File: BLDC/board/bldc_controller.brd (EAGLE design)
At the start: 104.1 x 76.8 mm, 113 parts, among them IC1 DRV8301, IC2 OPA2374, IC3 AS 5134, IC5 TPS51103, M1 FRDM-KL05Z, M2 MBED_NXP_LPC1768, Q1 MOSFET-NCHANNELSMD, Q2 MOSFET-NCHANNELSMD, Q3 P-CHANNEL-MOSFETTO252, Q4 SLPS388A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

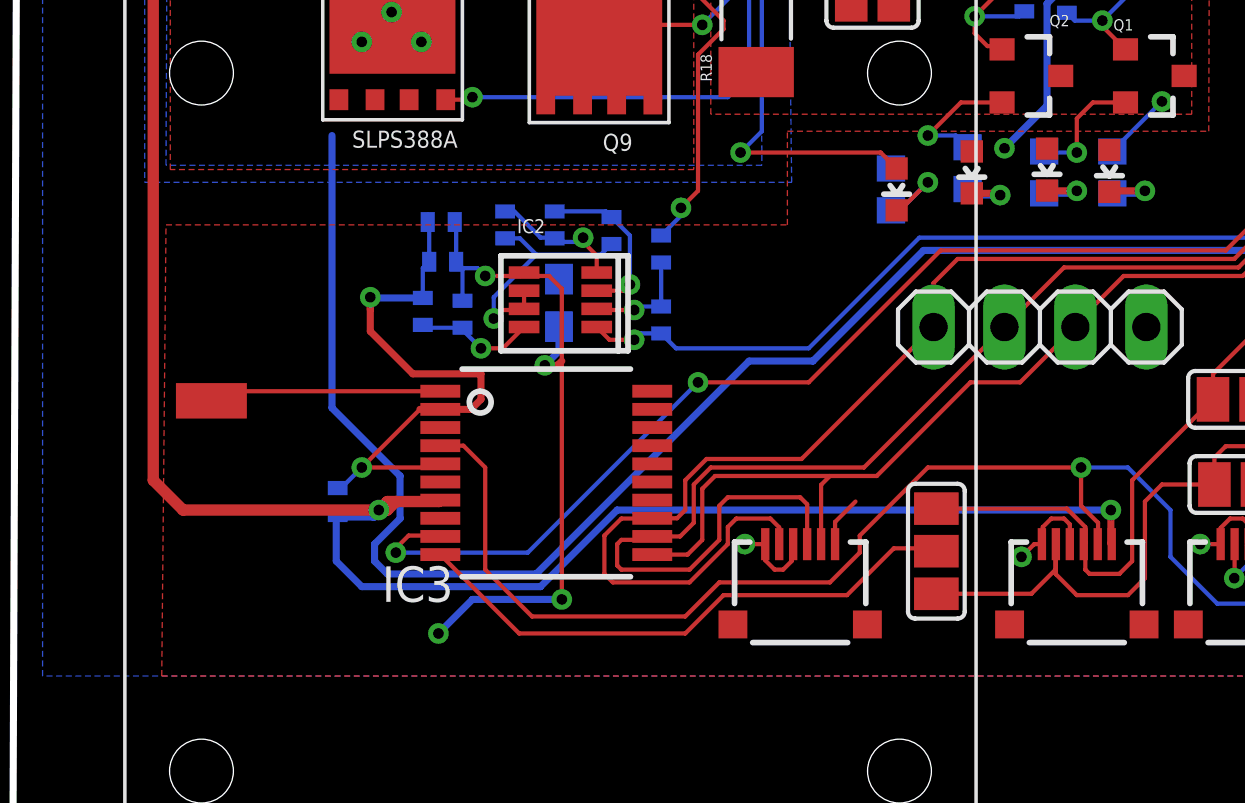
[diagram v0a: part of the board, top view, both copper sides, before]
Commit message: Fixed encoder alignment. May still need to fix holes for BLDC motor
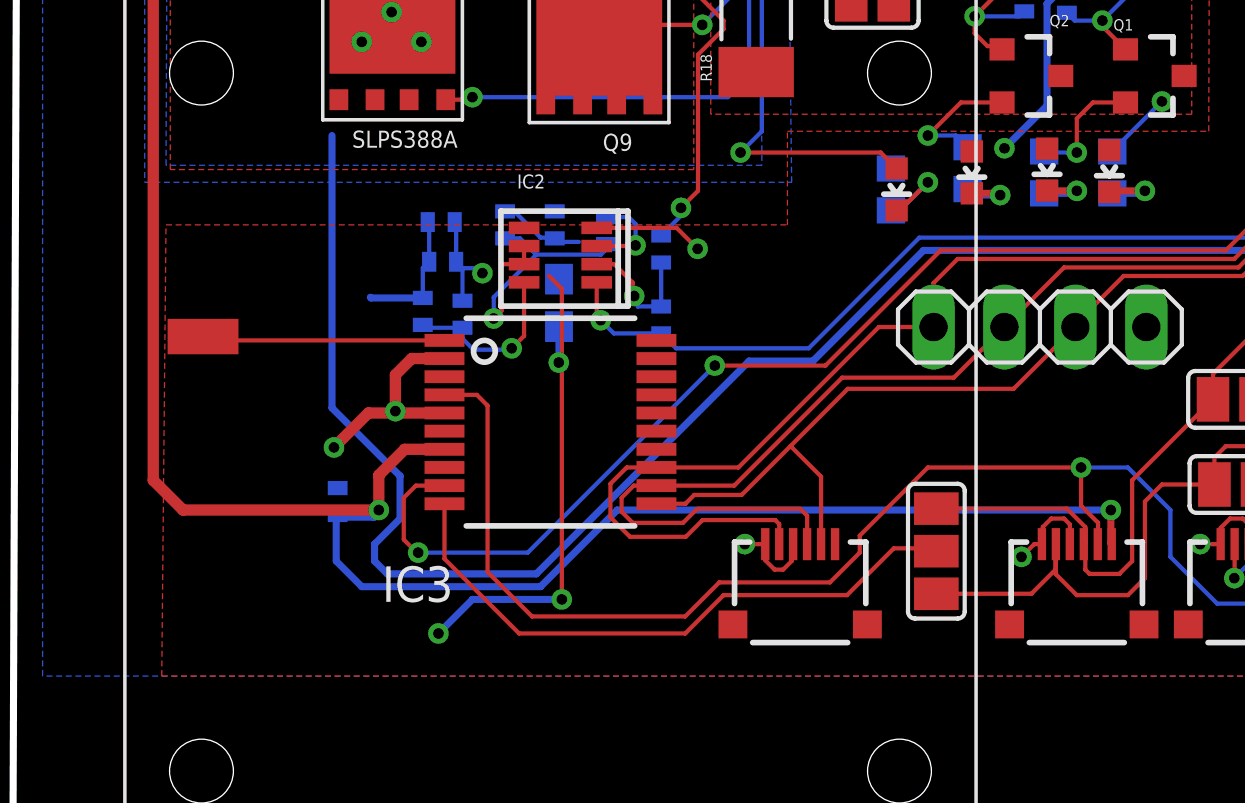
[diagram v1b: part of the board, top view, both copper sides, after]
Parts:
- IC3: device biomimetic:AS5134 -> modular_robotics:AS5134
- moved PAD9 2.32 mm to (6.81, 19.5)
- moved IC2 1.60 mm to (19.6, 21.4)
- moved R21 0.20 mm to (21.2, 23.3)
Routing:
- net GND: track 87.3 -> 80.2 mm
- net 3.3V: track 97.6 -> 92.2 mm
- net V: track 109.8 -> 105.9 mm
- net W: track 107.8 -> 105.0 mm
- net N$12: track 4.34 -> 6.35 mm
- net ENC_CS: track 158.1 -> 160.0 mm
- net ENC_DIO: track 20.2 -> 22.0 mm
- net N$14: track 9.01 -> 10.5 mm
- net C_I: track 119.2 -> 120.4 mm
- net ENC_CLK: track 101.2 -> 102.3 mm
- net N$16: track 3.95 -> 4.90 mm
- net 5V: track 113.0 -> 113.9 mm
- net N$15: track 6.08 -> 5.36 mm
- net U: track 103.7 -> 103.1 mm

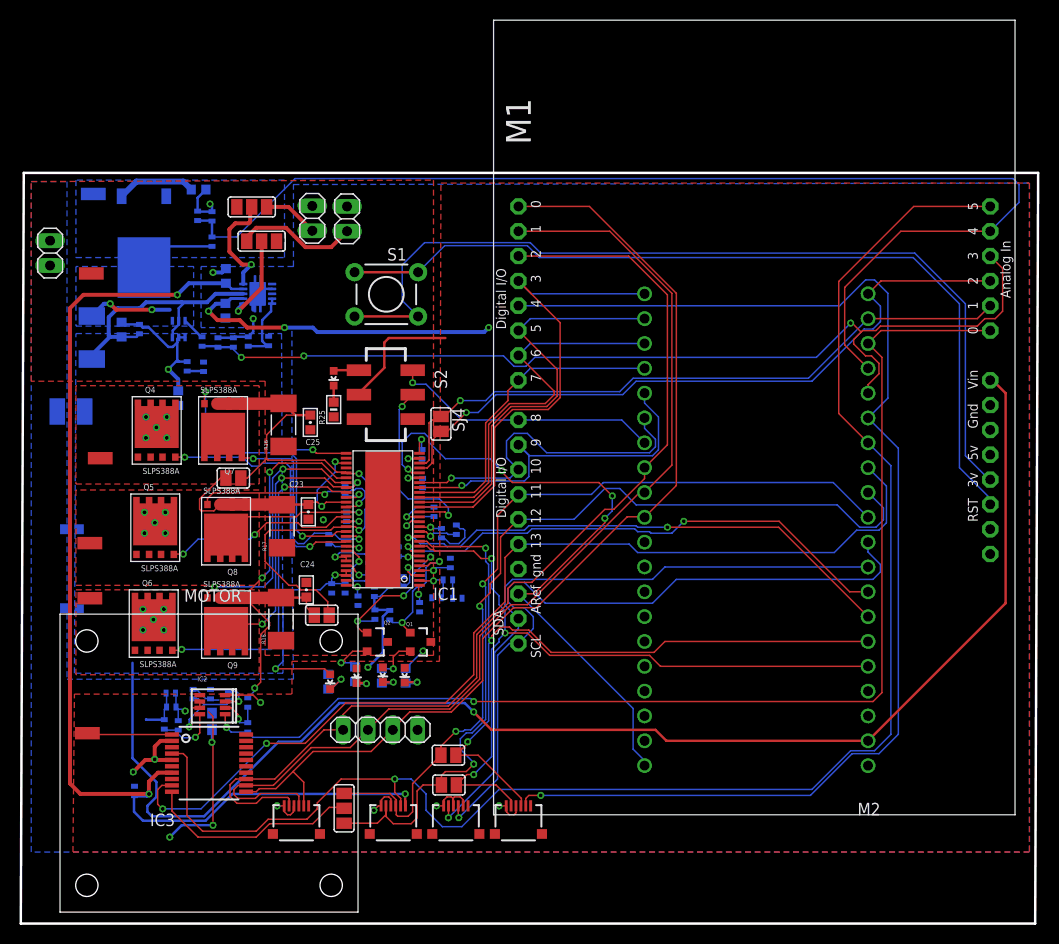
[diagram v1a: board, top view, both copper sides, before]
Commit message: Corrected BLDC mounting holes, added borders to boards, squeezed one more ADC board in to panelization
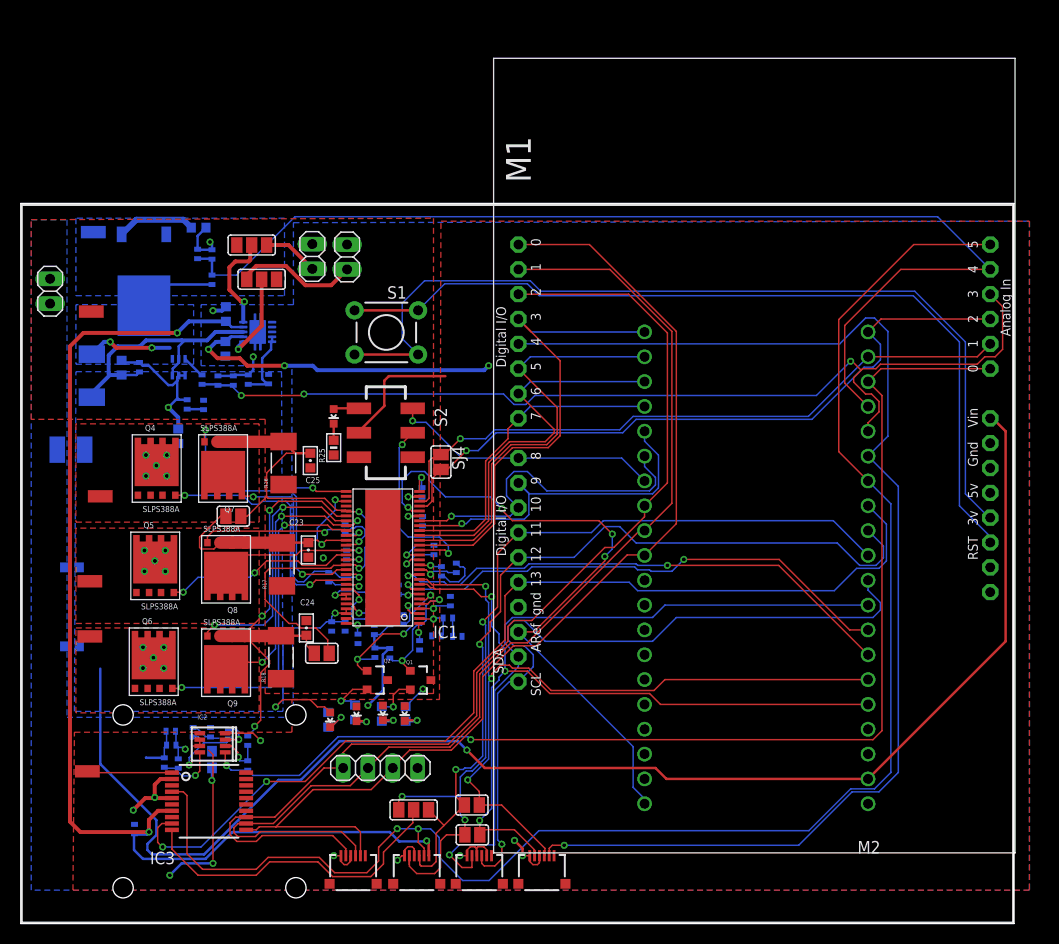
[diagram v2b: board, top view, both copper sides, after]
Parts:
- removed MOTOR: (no value), biomimetic:S-1804MOTOR
- added U$8: BLDC_MOUNT, modular_robotics:BLDC_MOUNT
- moved JP6 7.72 mm to (34.0, 5.21)
- moved SJ1 7.12 mm to (40.2, 11.6), turned to 180 degrees
- moved SJ2 5.64 mm to (46.1, 12.1)
- moved JP4 5.64 mm to (53.3, 5.21)
- moved JP5 5.64 mm to (40.5, 5.21)
- moved JP7 5.64 mm to (46.9, 5.21)
- moved SJ6 5.64 mm to (46.2, 9.07)
- moved C29 3.90 mm to (18.1, 68.5)
- moved C3 3.90 mm to (43.0, 36.0)
- moved C5 3.90 mm to (41.1, 41.2)
- moved C8 3.90 mm to (33.3, 37.7)
- moved C9 3.90 mm to (31.5, 35.4)
- moved JP3 3.90 mm to (33.4, 68.2)
- moved PAD1 3.90 mm to (8.13, 43.7)
- moved PAD4 3.90 mm to (7.21, 62.6)
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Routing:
- net ENC_DIO: track 22.0 -> 33.3 mm
- net U: track 103.1 -> 110.4 mm
- net SENSE_V_BATT: track 121.0 -> 114.0 mm
- net W: track 105.0 -> 111.3 mm
- net V: track 105.9 -> 112.2 mm
- net V_BATT: track 224.9 -> 230.1 mm
- net SDA: track 66.6 -> 71.2 mm
- net 5V: track 113.9 -> 116.9 mm
- net ENC_MISO: track 88.6 -> 85.7 mm
- net ENC_CS: track 160.0 -> 162.3 mm, vias 1 -> 2
- net CS_EXT: track 128.3 -> 126.4 mm
- net GND: track 80.2 -> 78.6 mm, vias 14 -> 15
- net DRV_MISO: track 80.4 -> 81.8 mm
- net ENC_MOSI: track 89.6 -> 90.7 mm, vias 2 -> 3
- net V5IN1: track 12.1 -> 11.1 mm
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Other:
- board size 104.1 x 76.8 mm -> 101.6 x 73.7 mm
